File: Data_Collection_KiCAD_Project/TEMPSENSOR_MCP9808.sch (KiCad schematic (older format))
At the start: 2 parts

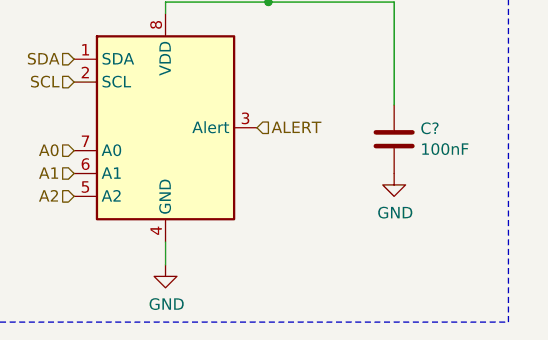
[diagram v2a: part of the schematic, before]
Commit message: Schematic v1.0.4
Added I2C addresses to MEMS, Temp Sensor, and Barometer on main schematic page.
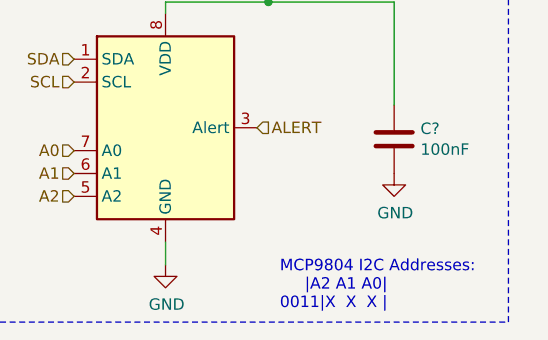
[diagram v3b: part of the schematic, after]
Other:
- note added: "MCP9804 I2C Addresses:\n |A2 A1 A0|\n0011|X X X |"
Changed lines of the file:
@@
 $Descr A4 11693 8268
 encoding utf-8
-Sheet 6 8
+Sheet 4 8
 Title "MCP9608 Temperature Sensor"
 Date "2021-10-01"
-Rev "v1.0.3"
+Rev "v1.0.4"
 Comp "Missouri S&T Rocket Design Team '21 (Thomas Francois)"
 Comment1 "https://github.com/MSTRocketDesignTeam/Avionics-Data-Collection-PCB"
@@
 Wire Wire Line
 	4250 2500 4250 2950
+Text Notes 3750 3850 0    50   ~ 0
+MCP9804 I2C Addresses:\n     |A2 A1 A0|\n0011|X  X  X |
 $EndSCHEMATC

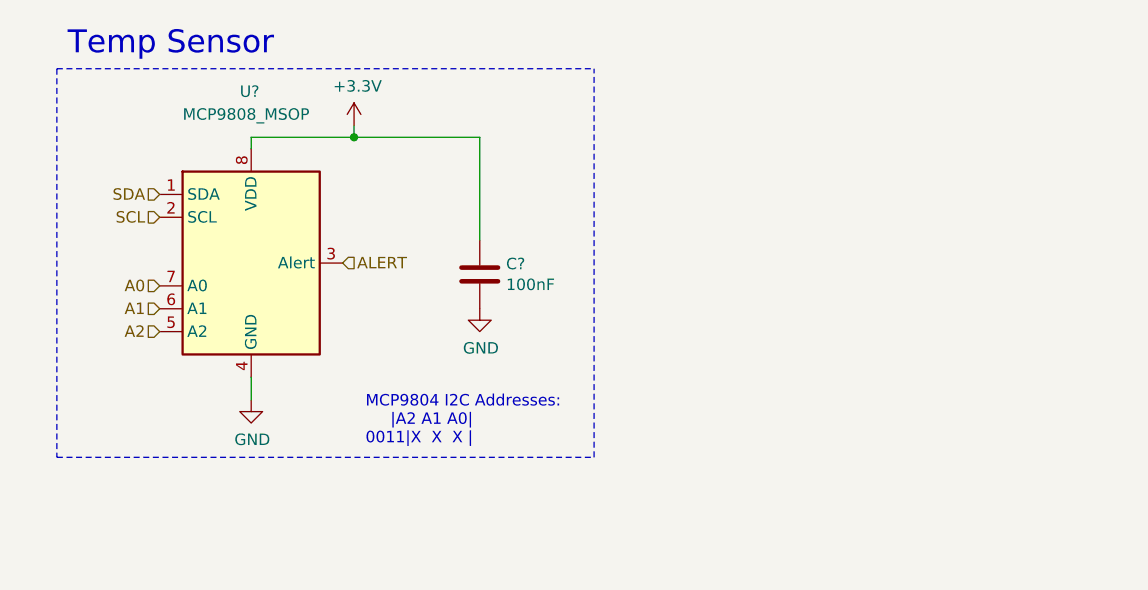
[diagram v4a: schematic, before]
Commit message: Separated BNO055 and KX134
Separated the hierarchical sheets for the BNO055 IMU and KX134 High G-Accelerometer.
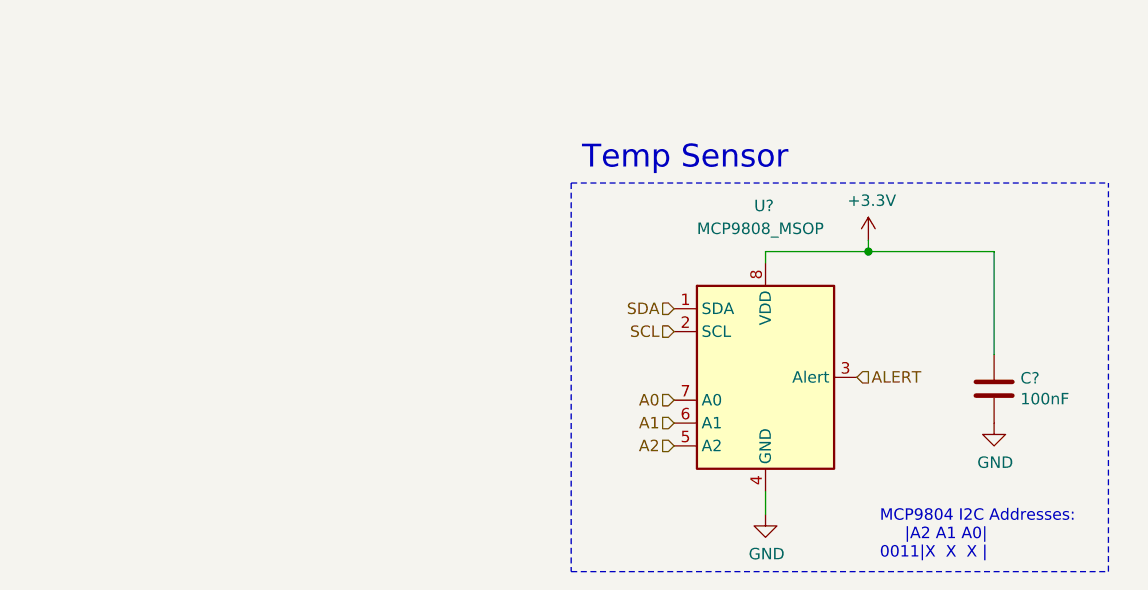
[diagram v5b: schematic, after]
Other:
- moved on the sheet: C?, U?
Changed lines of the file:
@@
 $Descr A4 11693 8268
 encoding utf-8
-Sheet 3 8
+Sheet 3 9
 Title "MCP9608 Temperature Sensor"
 Date "2021-10-01"
@@
 L power:GND #PWR?
 U 1 1 6160E311
-P 3250 3650
+P 5500 4150
 AR Path="/6160E311" Ref="#PWR?"  Part="1"
 AR Path="/615C1FB4/6160E311" Ref="#PWR?"  Part="1"
-F 0 "#PWR?" H 3250 3400 50  0001 C CNN
-F 1 "GND" H 3255 3477 50  0000 C CNN
-F 2 "" H 3250 3650 50  0001 C CNN
-F 3 "" H 3250 3650 50  0001 C CNN
-	1    3250 3650
+F 0 "#PWR?" H 5500 3900 50  0001 C CNN
+F 1 "GND" H 5505 3977 50  0000 C CNN
+F 2 "" H 5500 4150 50  0001 C CNN
+F 3 "" H 5500 4150 50  0001 C CNN
+	1    5500 4150
 	1    0    0    -1
 $EndComp
@@
 L power:+3.3V #PWR?
 U 1 1 6160E323
-P 3700 2450
+P 5950 2950
 AR Path="/6160E323" Ref="#PWR?"  Part="1"
 AR Path="/615C1FB4/6160E323" Ref="#PWR?"  Part="1"
-F 0 "#PWR?" H 3700 2300 50  0001 C CNN
-F 1 "+3.3V" H 3715 2623 50  0000 C CNN
-F 2 "" H 3700 2450 50  0001 C CNN
-F 3 "" H 3700 2450 50  0001 C CNN
-	1    3700 2450
+F 0 "#PWR?" H 5950 2800 50  0001 C CNN
+F 1 "+3.3V" H 5965 3123 50  0000 C CNN
+F 2 "" H 5950 2950 50  0001 C CNN
+F 3 "" H 5950 2950 50  0001 C CNN
+	1    5950 2950
 	1    0    0    -1
 $EndComp
 Wire Wire Line
-	3250 2550 3250 2500
+	5500 3050 5500 3000
 Wire Wire Line
-	3250 2500 3700 2500
+	5500 3000 5950 3000
 Wire Wire Line
-	3700 2500 3700 2450
+	5950 3000 5950 2950
 Wire Notes Line
-	2400 2200 2400 3900
-Text Notes 3350 2150 2    100  ~ 0
+	4650 2700 4650 4400
+Text Notes 5600 2650 2    100  ~ 0
 Temp Sensor
 $Comp
 L Device:C C?
 U 1 1 6160E331
-P 4250 3100
+P 6500 3600
 AR Path="/6160E331" Ref="C?"  Part="1"
 AR Path="/615C1FB4/6160E331" Ref="C?"  Part="1"
-F 0 "C?" H 4365 3146 50  0000 L CNN
-F 1 "100nF" H 4365 3055 50  0000 L CNN
-F 2 "" H 4288 2950 50  0001 C CNN
-F 3 "~" H 4250 3100 50  0001 C CNN
-	1    4250 3100
+F 0 "C?" H 6615 3646 50  0000 L CNN
+F 1 "100nF" H 6615 3555 50  0000 L CNN
+F 2 "" H 6538 3450 50  0001 C CNN
+F 3 "~" H 6500 3600 50  0001 C CNN
+	1    6500 3600
 	1    0    0    -1
 $EndComp
-Text HLabel 2850 2750 0    50   Input ~ 0
+Text HLabel 5100 3250 0    50   Input ~ 0
 SDA
-Text HLabel 2850 2850 0    50   Input ~ 0
+Text HLabel 5100 3350 0    50   Input ~ 0
 SCL
-Text HLabel 2850 3150 0    50   Input ~ 0
+Text HLabel 5100 3650 0    50   Input ~ 0
 A0
-Text HLabel 2850 3250 0    50   Input ~ 0
+Text HLabel 5100 3750 0    50   Input ~ 0
 A1
-Text HLabel 2850 3350 0    50   Input ~ 0
+Text HLabel 5100 3850 0    50   Input ~ 0
 A2
 Wire Wire Line
-	3250 3550 3250 3650
+	5500 4050 5500 4150
 $Comp
 L Sensor_Temperature:MCP9808_MSOP U?
 U 1 1 6160E30B
-P 3250 3050
+P 5500 3550
 AR Path="/6160E30B" Ref="U?"  Part="1"
 AR Path="/615C1FB4/6160E30B" Ref="U?"  Part="1"
-F 0 "U?" H 3200 3800 50  0000 L CNN
-F 1 "MCP9808_MSOP" H 2950 3700 50  0000 L CNN
-F 2 "Package_SO:MSOP-8_3x3mm_P0.65mm" H 3250 3050 50  0001 C CNN
-F 3 "http://ww1.microchip.com/downloads/en/DeviceDoc/22203b.pdf" H 3000 3500 50  0001 C CNN
-	1    3250 3050
+F 0 "U?" H 5450 4300 50  0000 L CNN
+F 1 "MCP9808_MSOP" H 5200 4200 50  0000 L CNN
+F 2 "Package_SO:MSOP-8_3x3mm_P0.65mm" H 5500 3550 50  0001 C CNN
+F 3 "http://ww1.microchip.com/downloads/en/DeviceDoc/22203b.pdf" H 5250 4000 50  0001 C CNN
+	1    5500 3550
 	1    0    0    -1
 $EndComp
 Wire Wire Line
-	3700 2500 4250 2500
-Connection ~ 3700 2500
+	5950 3000 6500 3000
+Connection ~ 5950 3000
 $Comp
 L power:GND #PWR?
 U 1 1 618848DE
-P 4250 3250
+P 6500 3750
 AR Path="/618848DE" Ref="#PWR?"  Part="1"
 AR Path="/615C1FB4/618848DE" Ref="#PWR?"  Part="1"
-F 0 "#PWR?" H 4250 3000 50  0001 C CNN
-F 1 "GND" H 4255 3077 50  0000 C CNN
-F 2 "" H 4250 3250 50  0001 C CNN
-F 3 "" H 4250 3250 50  0001 C CNN
-	1    4250 3250
+F 0 "#PWR?" H 6500 3500 50  0001 C CNN
+F 1 "GND" H 6505 3577 50  0000 C CNN
+F 2 "" H 6500 3750 50  0001 C CNN
+F 3 "" H 6500 3750 50  0001 C CNN
+	1    6500 3750
 	1    0    0    -1
 $EndComp
-Text HLabel 3650 3050 2    50   Input ~ 0
+Text HLabel 5900 3550 2    50   Input ~ 0
 ALERT
 Wire Notes Line
-	4750 3900 4750 2200
+	7000 4400 7000 2700
 Wire Notes Line
-	2400 3900 4750 3900
+	4650 4400 7000 4400
 Wire Notes Line
-	2400 2200 4750 2200
+	4650 2700 7000 2700
 Wire Wire Line
-	4250 2500 4250 2950
-Text Notes 3750 3850 0    50   ~ 0
+	6500 3000 6500 3450
+Text Notes 6000 4350 0    50   ~ 0
 MCP9804 I2C Addresses:\n     |A2 A1 A0|\n0011|X  X  X |
 $EndSCHEMATC

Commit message: Added Power Budget Spreadsheet
TODO:
-Implement I2C interrupt pin
-Add I2C Pullups
-Add I2C Capacitors
-Check for auxiliary pins needed from sensors
-Add power buffer cap and diode?
-Double check and finalize layouts
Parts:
- C?: symbol Device:C -> Data_Collection_KiCAD_Project-rescue:C-Device
- U?: symbol Sensor_Temperature:MCP9808_MSOP -> Data_Collection_KiCAD_Project-rescue:MCP9808_MSOP-Sensor_Temperature
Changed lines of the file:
@@
 $EndDescr
 $Comp
-L power:GND #PWR?
+L Data_Collection_KiCAD_Project-rescue:GND-power #PWR?
 U 1 1 6160E311
 P 5500 4150
@@
 $EndComp
 $Comp
-L power:+3.3V #PWR?
+L Data_Collection_KiCAD_Project-rescue:+3.3V-power #PWR?
 U 1 1 6160E323
 P 5950 2950
@@
 Temp Sensor
 $Comp
-L Device:C C?
+L Data_Collection_KiCAD_Project-rescue:C-Device C?
 U 1 1 6160E331
 P 6500 3600
@@
 	5500 4050 5500 4150
 $Comp
-L Sensor_Temperature:MCP9808_MSOP U?
+L Data_Collection_KiCAD_Project-rescue:MCP9808_MSOP-Sensor_Temperature U?
 U 1 1 6160E30B
 P 5500 3550
@@
 Connection ~ 5950 3000
 $Comp
-L power:GND #PWR?
+L Data_Collection_KiCAD_Project-rescue:GND-power #PWR?
 U 1 1 618848DE
 P 6500 3750
